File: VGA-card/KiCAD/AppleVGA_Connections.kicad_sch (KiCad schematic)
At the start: 7 parts, among them J1 AppleIIBus, J2 VGA, J3 VGA, SW1 SW_Push

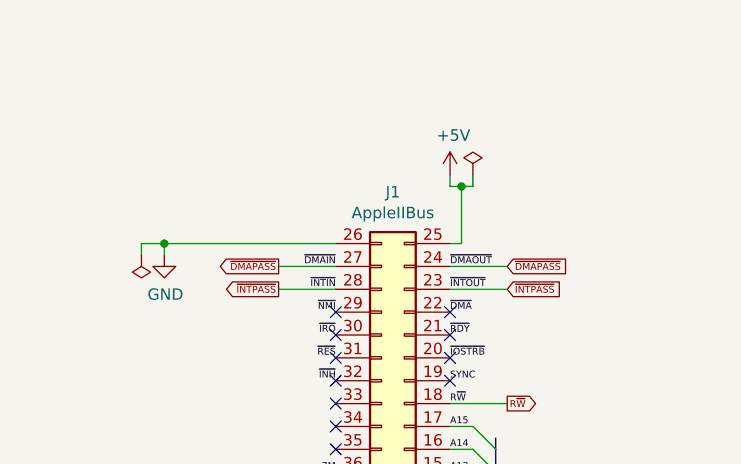
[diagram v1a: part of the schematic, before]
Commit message: KiCAD ERC errors have been fixed
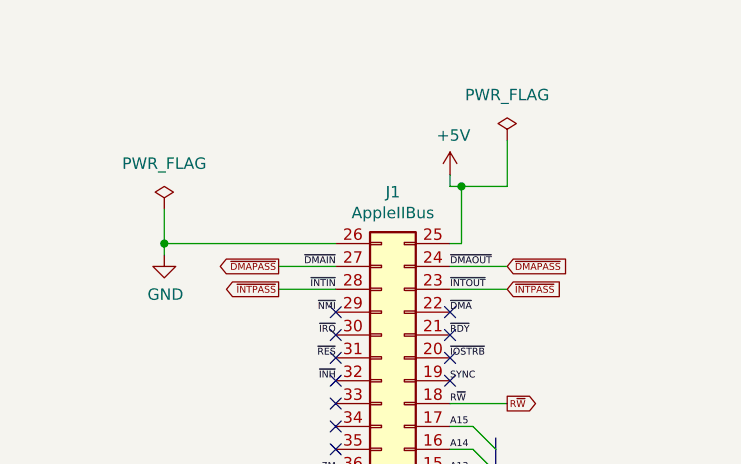
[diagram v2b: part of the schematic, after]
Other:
- title: Apple II VGA Card -> MPF-II VGA Card
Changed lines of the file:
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@@
   (paper "A4")
   (title_block
-    (title "Apple II VGA Card")
-    (date "2021-12-13")
+    (title "MPF-II VGA Card")
+    (date "2022-09-07")
     (rev "A")
     (comment 1 "Licensed under CERN-OHL-P V2.0 (https://ohwr.org/cern_ohl_p_v2.txt)")
     (comment 2 "Copyright (c) 2021-2022 Mark Aikens")
+    (comment 3 "Modified for MPF-II: The Random DIY (https://github.com/vitasam/mpf-ii_retro_6502)")
   )
   (junction (at 149.86 93.98) (diameter 0) (color 0 0 0 0)
   )
+  (junction (at 41.91 64.77) (diameter 0) (color 0 0 0 0)
+  )
   (junction (at 149.86 88.9) (diameter 0) (color 0 0 0 0)
   )
@@
   )
   (junction (at 39.37 173.99) (diameter 0) (color 0 0 0 0)
-  )
-  (junction (at 41.91 64.77) (diameter 0) (color 0 0 0 0)
   )
   (no_connect (at 60.96 77.47))
@@
     (stroke (width 0) (type default) (color 0 0 0 0))
   )
+  (wire (pts (xy 80.01 58.42) (xy 80.01 53.34))
+    (stroke (width 0) (type default) (color 0 0 0 0))
+  )
   (wire (pts (xy 73.66 58.42) (xy 73.66 57.15))
     (stroke (width 0) (type default) (color 0 0 0 0))
@@
     (stroke (width 0) (type default) (color 0 0 0 0))
   )
-  (wire (pts (xy 41.91 64.77) (xy 39.37 64.77))
-    (stroke (width 0) (type default) (color 0 0 0 0))
-  )
   (bus (pts (xy 78.74 110.49) (xy 78.74 113.03))
     (stroke (width 0) (type default) (color 0 0 0 0))
@@
     (stroke (width 0) (type default) (color 0 0 0 0))
   )
-  (wire (pts (xy 39.37 64.77) (xy 39.37 66.04))
-    (stroke (width 0) (type default) (color 0 0 0 0))
-  )
   (wire (pts (xy 58.42 107.95) (xy 60.96 107.95))
     (stroke (width 0) (type default) (color 0 0 0 0))
@@
     (stroke (width 0) (type default) (color 0 0 0 0))
   )
-  (wire (pts (xy 76.2 58.42) (xy 76.2 57.15))
-    (stroke (width 0) (type default) (color 0 0 0 0))
-  )
   (wire (pts (xy 58.42 120.65) (xy 60.96 120.65))
     (stroke (width 0) (type default) (color 0 0 0 0))
@@
     (stroke (width 0) (type default) (color 0 0 0 0))
   )
+  (wire (pts (xy 74.93 58.42) (xy 80.01 58.42))
+    (stroke (width 0) (type default) (color 0 0 0 0))
+  )
   (wire (pts (xy 74.93 58.42) (xy 73.66 58.42))
     (stroke (width 0) (type default) (color 0 0 0 0))
@@
     (stroke (width 0) (type default) (color 0 0 0 0))
   )
+  (wire (pts (xy 41.91 60.96) (xy 41.91 64.77))
+    (stroke (width 0) (type default) (color 0 0 0 0))
+  )
   (bus (pts (xy 78.74 90.17) (xy 78.74 92.71))
     (stroke (width 0) (type default) (color 0 0 0 0))
@@
   )
   (wire (pts (xy 76.2 123.19) (xy 73.66 123.19))
-    (stroke (width 0) (type default) (color 0 0 0 0))
-  )
-  (wire (pts (xy 74.93 58.42) (xy 76.2 58.42))
     (stroke (width 0) (type default) (color 0 0 0 0))
   )
@@
     (pin "1")
   )
-  (symbol (lib_id "power:PWR_FLAG") (at 76.2 57.15 0) (unit 1)
-    (in_bom yes) (on_board yes)
-    (property "Reference" "#FLG0101" (id 0) (at 76.2 55.245 0)
-      (effects (font (size 1.27 1.27)) hide)
-    )
-    (property "Value" "PWR_FLAG" (id 1) (at 76.2 52.7558 0)
-      (effects (font (size 1.27 1.27)) hide)
-    )
-    (property "Footprint" "" (id 2) (at 76.2 57.15 0)
-      (effects (font (size 1.27 1.27)) hide)
-    )
-    (property "Datasheet" "~" (id 3) (at 76.2 57.15 0)
-      (effects (font (size 1.27 1.27)) hide)
-    )
-    (pin "1")
-  )
-  (symbol (lib_id "power:PWR_FLAG") (at 39.37 66.04 180) (unit 1)
-    (in_bom yes) (on_board yes)
-    (property "Reference" "#FLG0102" (id 0) (at 39.37 67.945 0)
-      (effects (font (size 1.27 1.27)) hide)
-    )
-    (property "Value" "PWR_FLAG" (id 1) (at 39.37 70.4342 0)
-      (effects (font (size 1.27 1.27)) hide)
-    )
-    (property "Footprint" "" (id 2) (at 39.37 66.04 0)
-      (effects (font (size 1.27 1.27)) hide)
-    )
-    (property "Datasheet" "~" (id 3) (at 39.37 66.04 0)
-      (effects (font (size 1.27 1.27)) hide)
-    )
+  (symbol (lib_id "power:PWR_FLAG") (at 80.01 53.34 0) (unit 1)
+    (in_bom yes) (on_board yes) (fields_autoplaced)
+    (property "Reference" "#FLG02" (id 0) (at 80.01 51.435 0)
+      (effects (font (size 1.27 1.27)) hide)
+    )
+    (property "Value" "PWR_FLAG" (id 1) (at 80.01 48.26 0))
+    (property "Footprint" "" (id 2) (at 80.01 53.34 0)
+      (effects (font (size 1.27 1.27)) hide)
+    )
+    (property "Datasheet" "~" (id 3) (at 80.01 53.34 0)
+      (effects (font (size 1.27 1.27)) hide)
+    )
+    (pin "1")
+  )
+  (symbol (lib_id "power:PWR_FLAG") (at 41.91 60.96 0) (unit 1)
+    (in_bom yes) (on_board yes) (fields_autoplaced)
+    (property "Reference" "#FLG01" (id 0) (at 41.91 59.055 0)
+      (effects (font (size 1.27 1.27)) hide)
+    )
+    (property "Value" "PWR_FLAG" (id 1) (at 41.91 55.88 0))
+    (property "Footprint" "" (id 2) (at 41.91 60.96 0)
+      (effects (font (size 1.27 1.27)) hide)
+    )
+    (property "Datasheet" "~" (id 3) (at 41.91 60.96 0)
+      (effects (font (size 1.27 1.27)) hide)
+    )

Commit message: KiCAD error fixes
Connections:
- net +3V3 renamed +3.3V
- net 7M: no longer names the net of J1.36 (Pin_36)
- net PHI1: no longer names the net of J1.38 (Pin_38)
- net Q3: no longer names the net of J1.37 (Pin_37)
- net SYNC: no longer names the net of J1.19 (Pin_19)
- net ~{DMA}: no longer names the net of J1.22 (Pin_22)
- net ~{INH}: no longer names the net of J1.32 (Pin_32)
- net ~{IOSEL}: no longer names the net of J1.1 (Pin_1)
- net ~{IOSTRB}: no longer names the net of J1.20 (Pin_20)
- net ~{IRQ}: no longer names the net of J1.30 (Pin_30)
- net ~{NMI}: no longer names the net of J1.29 (Pin_29)
- net ~{RDY}: no longer names the net of J1.21 (Pin_21)
- net ~{RES}: no longer names the net of J1.31 (Pin_31)
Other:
- title: MPF-II VGA Card -> Apple II VGA Card
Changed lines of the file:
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@@
   (paper "A4")
   (title_block
-    (title "MPF-II VGA Card")
-    (date "2022-09-07")
+    (title "Apple II VGA Card")
+    (date "2022-09-08")
     (rev "A")
     (comment 1 "Licensed under CERN-OHL-P V2.0 (https://ohwr.org/cern_ohl_p_v2.txt)")
     (comment 2 "Copyright (c) 2021-2022 Mark Aikens")
-    (comment 3 "Modified for MPF-II: The Random DIY (https://github.com/vitasam/mpf-ii_retro_6502)")
   )
   (junction (at 149.86 93.98) (diameter 0) (color 0 0 0 0)
   )
+  (junction (at 149.86 88.9) (diameter 0) (color 0 0 0 0)
+  )
+  (junction (at 190.5 88.9) (diameter 0) (color 0 0 0 0)
+  )
+  (junction (at 199.39 109.22) (diameter 0) (color 0 0 0 0)
+  )
+  (junction (at 190.5 83.82) (diameter 0) (color 0 0 0 0)
+  )
   (junction (at 41.91 64.77) (diameter 0) (color 0 0 0 0)
   )
-  (junction (at 149.86 88.9) (diameter 0) (color 0 0 0 0)
-  )
-  (junction (at 190.5 88.9) (diameter 0) (color 0 0 0 0)
-  )
-  (junction (at 199.39 109.22) (diameter 0) (color 0 0 0 0)
-  )
-  (junction (at 190.5 83.82) (diameter 0) (color 0 0 0 0)
-  )
   (junction (at 190.5 101.6) (diameter 0) (color 0 0 0 0)
   )
@@
   )
   (no_connect (at 60.96 77.47))
+  (no_connect (at 60.96 95.25))
+  (no_connect (at 60.96 90.17))
+  (no_connect (at 60.96 87.63))
+  (no_connect (at 73.66 77.47))
+  (no_connect (at 73.66 80.01))
+  (no_connect (at 73.66 74.93))
+  (no_connect (at 73.66 72.39))
   (no_connect (at 60.96 74.93))
-  (no_connect (at 60.96 87.63))
-  (no_connect (at 73.66 80.01))
+  (no_connect (at 60.96 72.39))
   (no_connect (at 60.96 125.73))
-  (no_connect (at 60.96 95.25))
-  (no_connect (at 73.66 77.47))
   (no_connect (at 207.01 86.36))
   (no_connect (at 191.77 93.98))
-  (no_connect (at 60.96 90.17))
-  (no_connect (at 73.66 125.73))
-  (no_connect (at 73.66 72.39))
+  (no_connect (at 60.96 80.01))
   (no_connect (at 60.96 82.55))
   (no_connect (at 207.01 81.28))
   (no_connect (at 60.96 97.79))
   (no_connect (at 191.77 96.52))
+  (no_connect (at 207.01 101.6))
   (no_connect (at 60.96 92.71))
-  (no_connect (at 207.01 101.6))
-  (no_connect (at 60.96 72.39))
-  (no_connect (at 60.96 80.01))
   (no_connect (at 60.96 85.09))
-  (no_connect (at 73.66 74.93))
+  (no_connect (at 73.66 125.73))
   (bus_entry (at 76.2 113.03) (size 2.54 2.54)
     (stroke (width 0) (type default) (color 0 0 0 0))
@@
     (stroke (width 0) (type default) (color 0 0 0 0))
   )
-  (wire (pts (xy 80.01 58.42) (xy 80.01 53.34))
-    (stroke (width 0) (type default) (color 0 0 0 0))
-  )
   (wire (pts (xy 73.66 58.42) (xy 73.66 57.15))
     (stroke (width 0) (type default) (color 0 0 0 0))
@@
     (stroke (width 0) (type default) (color 0 0 0 0))
   )
+  (wire (pts (xy 76.2 50.8) (xy 76.2 58.42))
+    (stroke (width 0) (type default) (color 0 0 0 0))
+  )
   (wire (pts (xy 58.42 120.65) (xy 60.96 120.65))
     (stroke (width 0) (type default) (color 0 0 0 0))
@@
     (stroke (width 0) (type default) (color 0 0 0 0))
   )
-  (wire (pts (xy 74.93 58.42) (xy 80.01 58.42))
-    (stroke (width 0) (type default) (color 0 0 0 0))
-  )
   (wire (pts (xy 74.93 58.42) (xy 73.66 58.42))
     (stroke (width 0) (type default) (color 0 0 0 0))
@@
     (stroke (width 0) (type default) (color 0 0 0 0))
   )
+  (bus (pts (xy 78.74 90.17) (xy 78.74 92.71))
+    (stroke (width 0) (type default) (color 0 0 0 0))
+  )
+  (wire (pts (xy 76.2 97.79) (xy 73.66 97.79))
+    (stroke (width 0) (type default) (color 0 0 0 0))
+  )
+  (wire (pts (xy 190.5 101.6) (xy 191.77 101.6))
+    (stroke (width 0) (type default) (color 0 0 0 0))
+  )
+  (bus (pts (xy 55.88 118.11) (xy 55.88 120.65))
+    (stroke (width 0) (type default) (color 0 0 0 0))
+  )
   (wire (pts (xy 41.91 60.96) (xy 41.91 64.77))
     (stroke (width 0) (type default) (color 0 0 0 0))
   )
-  (bus (pts (xy 78.74 90.17) (xy 78.74 92.71))
-    (stroke (width 0) (type default) (color 0 0 0 0))
-  )
-  (wire (pts (xy 76.2 97.79) (xy 73.66 97.79))
-    (stroke (width 0) (type default) (color 0 0 0 0))
-  )
-  (wire (pts (xy 190.5 101.6) (xy 191.77 101.6))
-    (stroke (width 0) (type default) (color 0 0 0 0))
-  )
-  (bus (pts (xy 55.88 118.11) (xy 55.88 120.65))
-    (stroke (width 0) (type default) (color 0 0 0 0))
-  )
   (wire (pts (xy 191.77 91.44) (xy 187.96 91.44))
     (stroke (width 0) (type default) (color 0 0 0 0))
@@
     (stroke (width 0) (type default) (color 0 0 0 0))
   )
+  (wire (pts (xy 74.93 58.42) (xy 76.2 58.42))
+    (stroke (width 0) (type default) (color 0 0 0 0))
+  )
   (wire (pts (xy 151.13 83.82) (xy 149.86 83.82))
     (stroke (width 0) (type default) (color 0 0 0 0))
@@
     (effects (font (size 0.762 0.762)) (justify right bottom))
   )
-  (label "~{RES}" (at 60.96 77.47 180)
-    (effects (font (size 0.762 0.762)) (justify right bottom))
-  )
   (label "PHI0" (at 60.96 100.33 180)
     (effects (font (size 0.762 0.762)) (justify right bottom))
@@
     (effects (font (size 0.762 0.762)) (justify right bottom))
   )
-  (label "~{RDY}" (at 73.66 74.93 0)
-    (effects (font (size 0.762 0.762)) (justify left bottom))
-  )
-  (label "SYNC" (at 73.66 80.01 0)
-    (effects (font (size 0.762 0.762)) (justify left bottom))
-  )
   (label "A0" (at 73.66 123.19 0)
     (effects (font (size 0.762 0.762)) (justify left bottom))
@@
     (effects (font (size 0.762 0.762)) (justify left bottom))
   )
-  (label "~{IOSEL}" (at 73.66 125.73 0)
-    (effects (font (size 0.762 0.762)) (justify left bottom))
-  )
   (label "A11" (at 73.66 95.25 0)
     (effects (font (size 0.762 0.762)) (justify left bottom))
   )
-  (label "~{IRQ}" (at 60.96 74.93 180)
-    (effects (font (size 0.762 0.762)) (justify right bottom))
-  )
-  (label "PHI1" (at 60.96 95.25 180)
-    (effects (font (size 0.762 0.762)) (justify right bottom))
-  )
   (label "A5" (at 73.66 110.49 0)
     (effects (font (size 0.762 0.762)) (justify left bottom))
@@
     (effects (font (size 0.762 0.762)) (justify left bottom))
   )
-  (label "Q3" (at 60.96 92.71 180)
-    (effects (font (size 0.762 0.762)) (justify right bottom))
-  )
   (label "A13" (at 73.66 90.17 0)
     (effects (font (size 0.762 0.762)) (justify left bottom))
@@
     (effects (font (size 0.762 0.762)) (justify right bottom))
   )
-  (label "~{DMA}" (at 73.66 72.39 0)
-    (effects (font (size 0.762 0.762)) (justify left bottom))
-  )
   (label "A1" (at 73.66 120.65 0)
     (effects (font (size 0.762 0.762)) (justify left bottom))
@@
     (effects (font (size 0.762 0.762)) (justify right bottom))
   )
-  (label "~{NMI}" (at 60.96 72.39 180)
-    (effects (font (size 0.762 0.762)) (justify right bottom))
-  )
   (label "~{INTIN}" (at 60.96 69.85 180)
     (effects (font (size 0.762 0.762)) (justify right bottom))
@@
     (effects (font (size 0.762 0.762)) (justify left bottom))
   )
-  (label "~{INH}" (at 60.96 80.01 180)
-    (effects (font (size 0.762 0.762)) (justify right bottom))
-  )
   (label "~{INTOUT}" (at 73.66 69.85 0)
     (effects (font (size 0.762 0.762)) (justify left bottom))
   )
-  (label "7M" (at 60.96 90.17 180)
-    (effects (font (size 0.762 0.762)) (justify right bottom))
-  )
   (label "A8" (at 73.66 102.87 0)
     (effects (font (size 0.762 0.762)) (justify left bottom))
@@
   (label "~{DEVSEL}" (at 60.96 102.87 180)
     (effects (font (size 0.762 0.762)) (justify right bottom))
-  )
-  (label "~{IOSTRB}" (at 73.66 77.47 0)
-    (effects (font (size 0.762 0.762)) (justify left bottom))
   )
   (label "A6" (at 73.66 107.95 0)
@@
     (pin "2")
   )
-  (symbol (lib_id "AppleVGA-rescue:+3.3V-power") (at 39.37 166.37 0) (unit 1)
+  (symbol (lib_id "power:+3.3V") (at 39.37 166.37 0) (unit 1)
     (in_bom yes) (on_board yes)
     (property "Reference" "#PWR0115" (id 0) (at 39.37 170.18 0)
@@
     (pin "1")
   )
-  (symbol (lib_id "power:PWR_FLAG") (at 80.01 53.34 0) (unit 1)
+  (symbol (lib_id "power:PWR_FLAG") (at 76.2 50.8 0) (unit 1)
     (in_bom yes) (on_board yes) (fields_autoplaced)
-    (property "Reference" "#FLG02" (id 0) (at 80.01 51.435 0)
-      (effects (font (size 1.27 1.27)) hide)
-    )
-    (property "Value" "PWR_FLAG" (id 1) (at 80.01 48.26 0))
-    (property "Footprint" "" (id 2) (at 80.01 53.34 0)
-      (effects (font (size 1.27 1.27)) hide)
-    )
-    (property "Datasheet" "~" (id 3) (at 80.01 53.34 0)
-      (effects (font (size 1.27 1.27)) hide)
-    )
+    (property "Reference" "#FLG02" (id 0) (at 76.2 48.895 0)
+      (effects (font (size 1.27 1.27)) hide)
+    )
+    (property "Value" "PWR_FLAG" (id 1) (at 76.2 45.72 0))
+    (property "Footprint" "" (id 2) (at 76.2 50.8 0)
+      (effects (font (size 1.27 1.27)) hide)
+    )
+    (property "Datasheet" "~" (id 3) (at 76.2 50.8 0)
+      (effects (font (size 1.27 1.27)) hide)
+    )
